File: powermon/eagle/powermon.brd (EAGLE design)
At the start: 50 x 50 mm, 46 parts, among them J1 USB, J3 TERMINAL-2, J6 USB, U1 LTC2943, U2 LT1764AEQ, U3 FT232RLQFN32, U4 ATMEGA328MLF

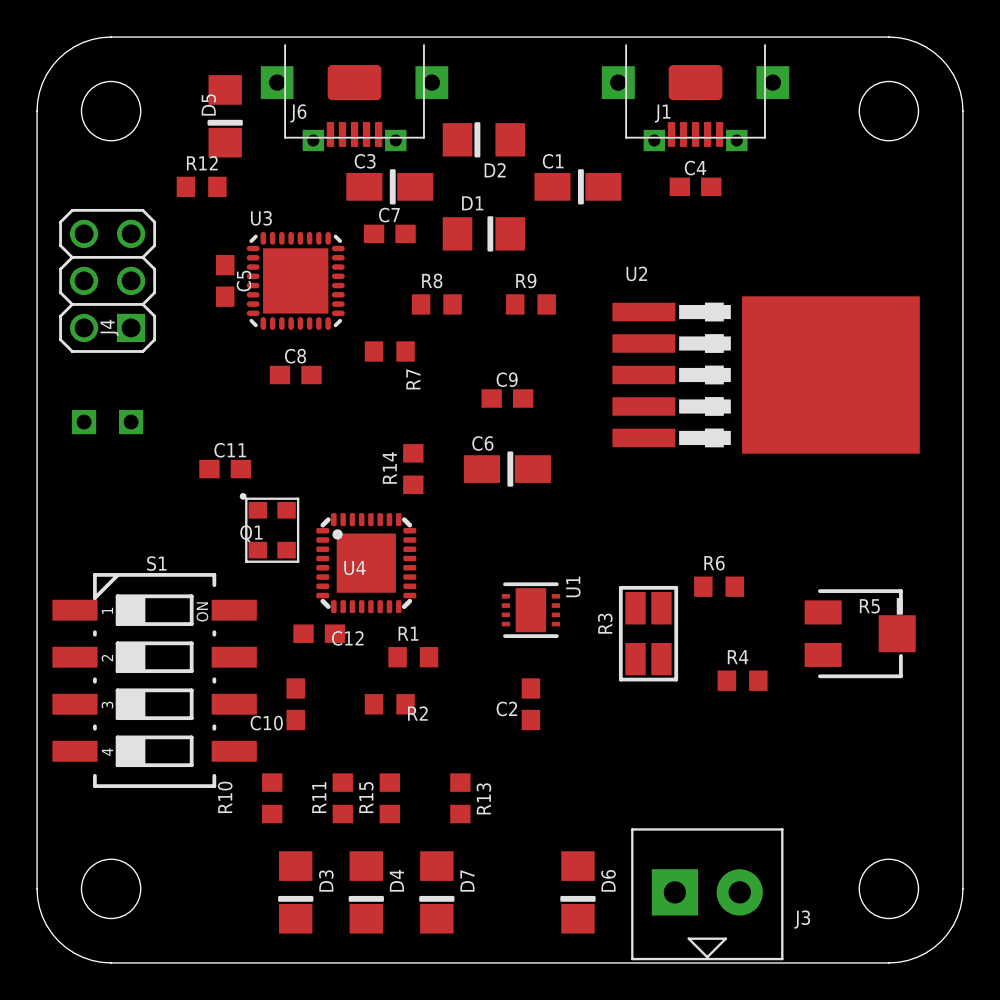
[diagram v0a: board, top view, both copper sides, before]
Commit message: Done initial routing of manual nets. Incomplete.
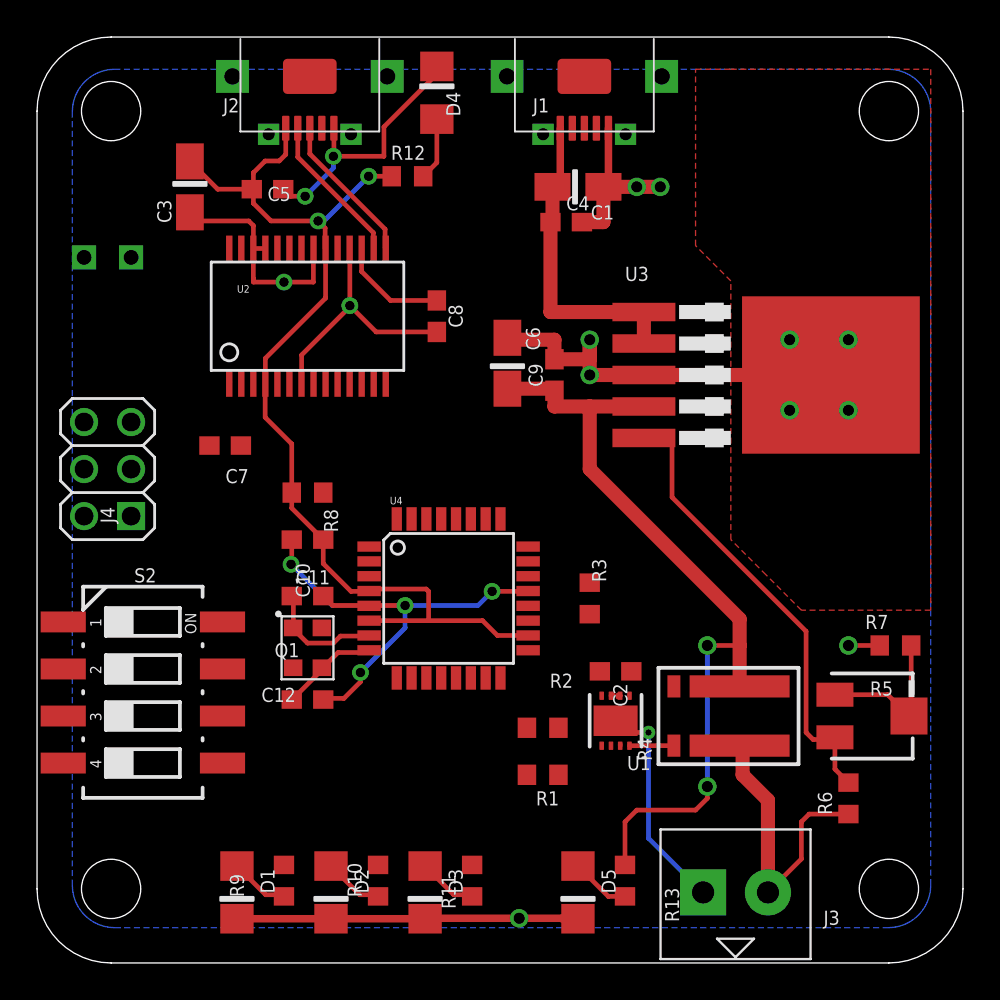
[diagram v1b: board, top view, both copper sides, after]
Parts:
- removed D6: BLUE, powermon:1206-LED
- removed D7: GREEN, powermon:1206-LED
- removed J6: USB, powermon:ZX62RD-AB-5P8
- removed R14: 10K, powermon:R0603
- removed R15: 3.3K, powermon:R0603
- removed S3: PUSH_BUTTON, powermon:DUMMY-2
- added J2: USB, powermon:ZX62RD-AB-5P8
- added S2: 219-04, powermon:CTS-219-04
- D3: value RED -> GREEN
- D4: value GREEN -> BLUE
- R1: value 4.7K -> 10K
- R3: value 0.025R 1% -> 4.7K; device powermon:SHUNT -> powermon:R0603
- R4: value 8K2 1% -> 0.025R 1%; device powermon:R0603 -> powermon:SHUNT
- R6: value 3.3K 1% -> 8K2 1%
- R7: value 10K -> 3.3K 1%
- R8: value 3.3K -> 10K
- S1: value 219-04 -> PUSH_BUTTON; device powermon:CTS-219-04 -> powermon:DUMMY-2
- U2: value LT1764AEQ -> FT232RL; device powermon:TO263-5 -> powermon:SSOP28DB
- U3: value FT232RLQFN32 -> LT1764AEQ; device powermon:QFN32 -> powermon:TO263-5
- U4: value ATMEGA328MLF -> ATMEGA328TQFP32; device powermon:MLF32 -> powermon:TQFP32-08
- moved D5 46.0 mm to (29.2, 3.81)
- moved D4 43.3 mm to (21.6, 47.0), turned to 90 degrees
- moved D2 41.5 mm to (15.9, 3.81), turned to 270 degrees
- moved D1 38.0 mm to (10.8, 3.81), turned to 270 degrees
- moved R9 33.9 mm to (13.3, 4.45), turned to 90 degrees
- moved R7 31.6 mm to (46.4, 17.1)
- moved U3 25.9 mm to (39.4, 31.8), turned to 270 degrees
- moved U2 25.0 mm to (14.6, 34.9), turned to 0 degrees
- moved S1 24.2 mm to (5.08, 39.4), turned to 0 degrees
- moved C7 14.5 mm to (10.2, 27.9), turned to 180 degrees
- moved R6 13.4 mm to (43.8, 8.89), turned to 90 degrees
- moved R8 12.3 mm to (14.6, 25.4), turned to 180 degrees
- moved R12 11.1 mm to (20.0, 42.5)
- moved C3 10.8 mm to (8.26, 41.9), turned to 90 degrees
- moved J4 10.2 mm to (3.81, 26.7)
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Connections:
- removed net GND@3: U1.2, U1.3, U1.7, U1.EXP
- removed net N$12: C3.+, C5.1, J6.1, U3.1, U3.19
- removed net N$21: J1.1
- removed net N$6: D1.A, R8.1
- removed net N$8: D2.A, R9.1
- removed net RX_LED: D2.C, U3.22
- removed net TX_LED: D1.C, U3.21
- net +5V: now also C3.+, C5.1, J2.1, R3.2, U2.20, U2.4; no longer R14.2, R7.2, R9.2
- net ACTION: now also S1.P$1; no longer S3.P$1
- net ACTIVITY_LED: now also R10.2; no longer R11.2
- net CONFIG1: now also S2.8; no longer S1.8
- net CONFIG2: now also S2.7; no longer S1.7
- net CONFIG3: now also S2.6; no longer S1.6
- net CONFIG4: now also S2.5; no longer S1.5
- net DEBUG_LED: now also R11.2; no longer R15.2
- net ERROR_LED: now also R9.2; no longer R10.2
- net GND: now also D1.C, D2.C, J2.5, R7.2, S1.P$2, S2.1, S2.2, S2.3, S2.4, U1.2, U1.3, U1.7, U1.EXP, U2.18, U2.21, U2.25, U2.26, U2.7, U3.3, U3.6; no longer D6.C, D7.C, J6.5, R6.2, S1.1, S1.2, S1.3, S1.4, S3.P$2, U2.3, U2.6, U3.17, U3.20, U3.24, U3.26, U3.4, U3.EXP, U4.EXP
- net I2C-CLK: now also R3.1; no longer R2.1
- net I2C-DATA: now also R2.1; no longer R1.1
- net N$1: now also R1.1; no longer R14.1
- net N$10: now also J2.3, U2.15; no longer J6.3, U3.14
- net N$11: now also U2.2; no longer U3.31
- net N$14: now also D5.A; no longer D6.A
- net N$15: now also J2.2, U2.16; no longer J6.2, U3.15
- net N$16: now also U2.17; no longer U3.16
- net N$17: now also D4.A; no longer D5.A
- net N$18: now also R7.1; no longer R6.1
- net N$19: now also R6.2, U3.5; no longer R4.2, U2.5
- net N$20: now also D3.A, R11.1; no longer D7.A, R15.1
- net N$22: now also R4.I1, R6.1; no longer R3.I1, R4.1
- net N$3: now also D2.A, R10.1; no longer D4.A, R11.1
- net N$4: now also D1.A, R9.1; no longer D3.A, R10.1
- net N$9: now also J1.1, U3.1, U3.2; no longer U2.1, U2.2
- net RESET: now also R8.1; no longer R7.1
- net SENSE+: now also R4.V2; no longer R3.V2
- net SENSE-: now also R4.V1; no longer R3.V1
- net SER_RX: now also U2.1; no longer U3.30
- net SER_TX: now also U2.5; no longer U3.2
- net V+: now also R4.I2, U3.4; no longer R3.I2, U2.4
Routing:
- net GND: track 1.41 -> 135.1 mm, vias 0 -> 19
- net +5V: track 0.00 -> 56.4 mm, vias 0 -> 2
- net V+: track 0.00 -> 45.8 mm, vias 0 -> 2
- net N$19: track 0.00 -> 25.5 mm
- net N$9: track 0.00 -> 16.1 mm
- net N$22: track 0.00 -> 15.8 mm
- net N$18: track 0.00 -> 8.34 mm
- net N$10: track 0.00 -> 8.19 mm
- net N$15: track 0.00 -> 7.70 mm
- net N$2: track 0.00 -> 6.39 mm
- net N$16: track 0.00 -> 5.96 mm
- net N$7: track 0.00 -> 4.82 mm
- net N$20: track 0.00 -> 4.01 mm
- net N$4: track 0.00 -> 4.01 mm
- net N$3: track 0.00 -> 4.01 mm
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- added copper zone on layer 1, net GND
- added copper zone on layer 16, net GND

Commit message: Added footprints, tweaked the placement. Work in progress.
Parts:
- S1: value PUSH_BUTTON -> PUSH_BUTTONEVQPSL; device powermon:DUMMY-2 -> powermon:EVQPSL
- moved S1 3.70 mm to (3.17, 36.2), turned to 180 degrees
- moved J4 2.74 mm to (6.54, 26.5)
- moved C7 1.09 mm to (11.0, 27.3), turned to 270 degrees
- moved S2 0.72 mm to (6.22, 15.1)
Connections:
- net ACTION: now also S1.2.1; no longer S1.P$1
- net GND: now also S1.1.1; no longer S1.P$2
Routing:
- removed copper zone on layer 1, net GND

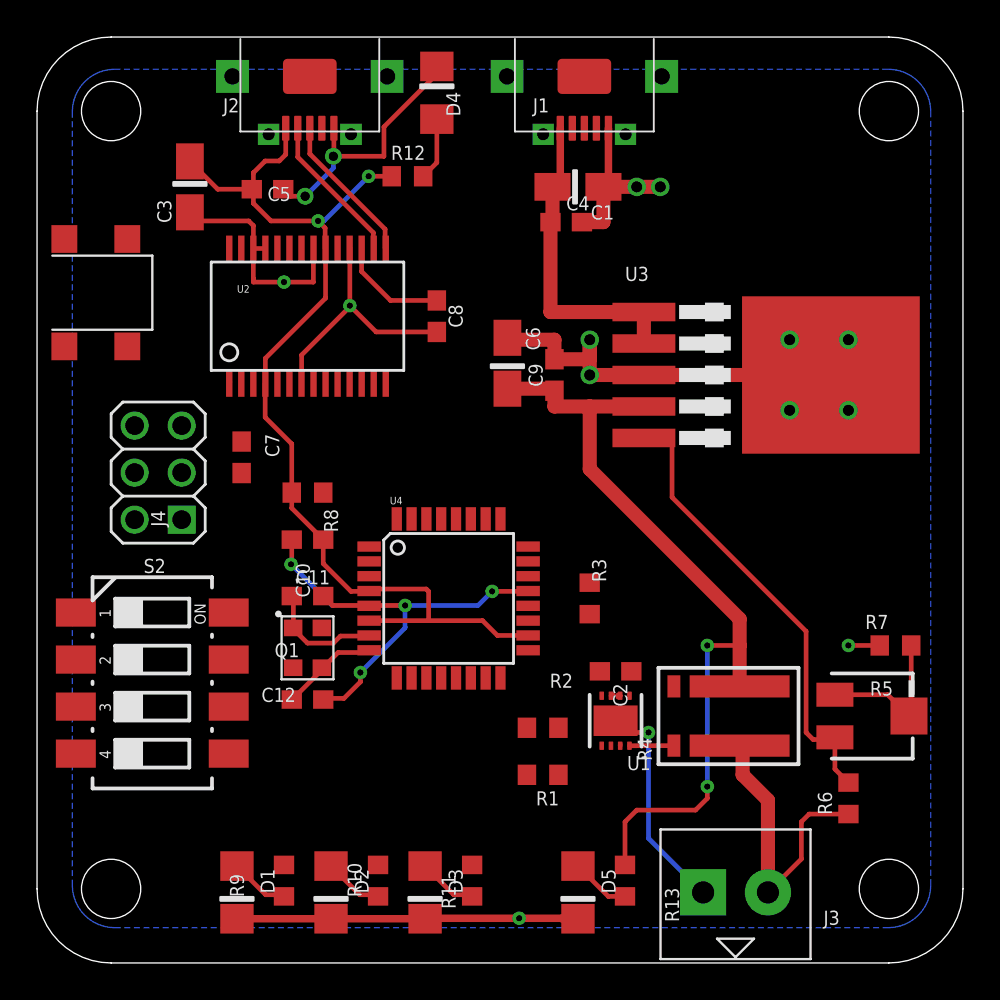
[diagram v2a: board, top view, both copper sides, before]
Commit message: Tweaked the board layout. No DRC. Almost ready for final auto routing.
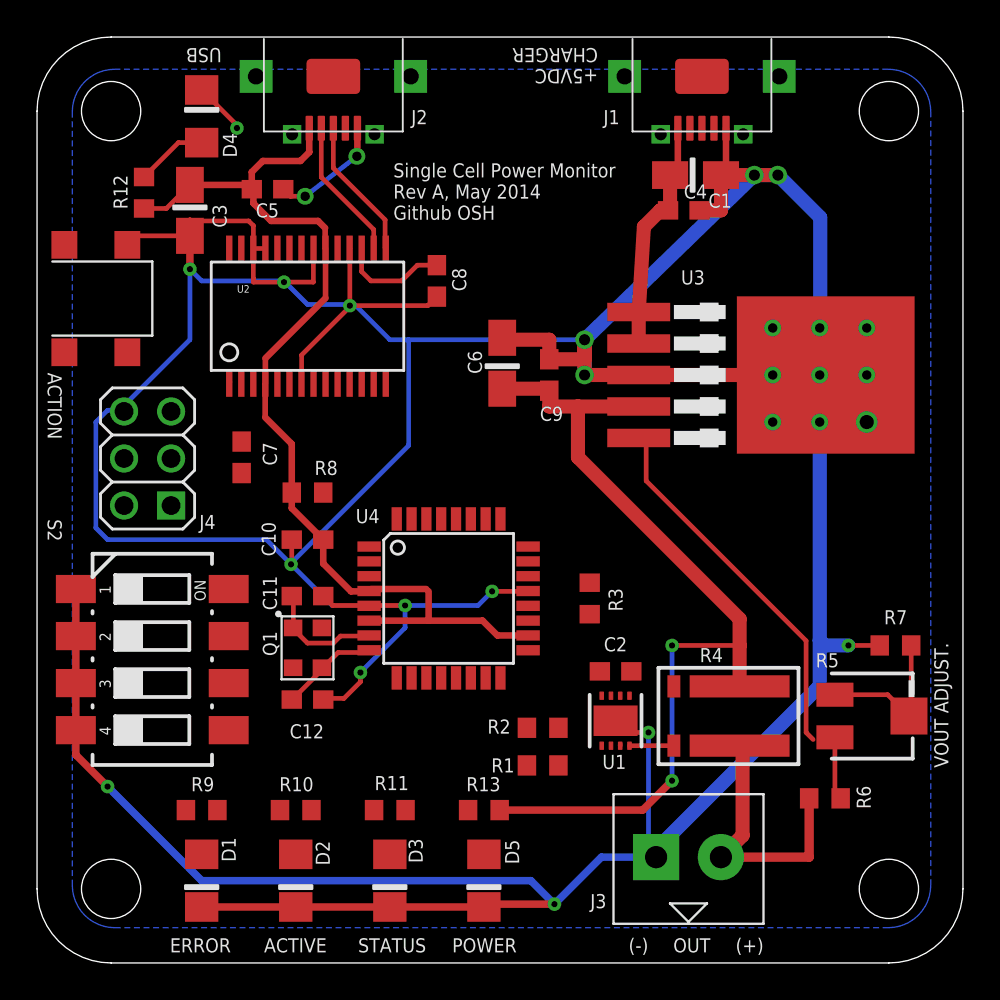
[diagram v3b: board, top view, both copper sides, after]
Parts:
- J1, J2: device powermon:ZX62RD-AB-5P8 -> powermon:USB-MICRO-ZX62RD-AB-5P8
- S1: device powermon:EVQPSL -> powermon:EVQPSL-PUSH-BUTTON
- moved R12 14.3 mm to (5.78, 41.6), turned to 90 degrees
- moved D4 12.8 mm to (8.89, 45.7)
- moved R13 8.52 mm to (24.1, 8.26), turned to 180 degrees
- moved C1 6.38 mm to (35.6, 42.5)
- moved C4 6.38 mm to (34.9, 40.6)
- moved J1 6.35 mm to (35.9, 50.5)
- moved R11 5.85 mm to (19.1, 8.26), turned to 0 degrees
- moved R9 5.85 mm to (8.89, 8.26), turned to 0 degrees
- moved R10 5.85 mm to (14.0, 8.26), turned to 0 degrees
- moved D5 5.12 mm to (24.1, 4.45)
- moved J3 3.17 mm to (35.2, 5.71)
- moved D1 2.01 mm to (8.89, 4.45)
- moved D2 2.01 mm to (14.0, 4.45)
- moved D3 2.01 mm to (19.1, 4.45)
- moved C8 1.91 mm to (21.6, 36.8)
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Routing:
- net GND: track 135.1 -> 326.5 mm, vias 19 -> 27
- net N$9: track 16.1 -> 12.0 mm
- net N$20: track 4.01 -> 0.00 mm
- net N$4: track 4.01 -> 0.00 mm
- net N$3: track 4.01 -> 0.00 mm
- net V+: track 45.8 -> 49.7 mm
- net N$14: track 3.22 -> 0.00 mm
- net N$22: track 15.8 -> 14.5 mm
- net +5V: track 56.4 -> 55.1 mm, vias 2 -> 0
- net N$10: track 8.19 -> 7.67 mm
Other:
- board text added: "(+)"
- board text added: "(-)"
- board text added: "+5VDC CHARGER"
- board text added: "ACTION"
- board text added: "ACTIVE"
- board text added: "ERROR"
- board text added: "OUT"
- board text added: "POWER"
- board text added: "STATUS"
- board text added: "Single Cell Power Monitor Rev A, May 2014 Github OSH"
- board text added: "USB"
- board text added: "VOUT ADJUST."

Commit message: Cleaned up the layout. Should be ready for final auto routing.
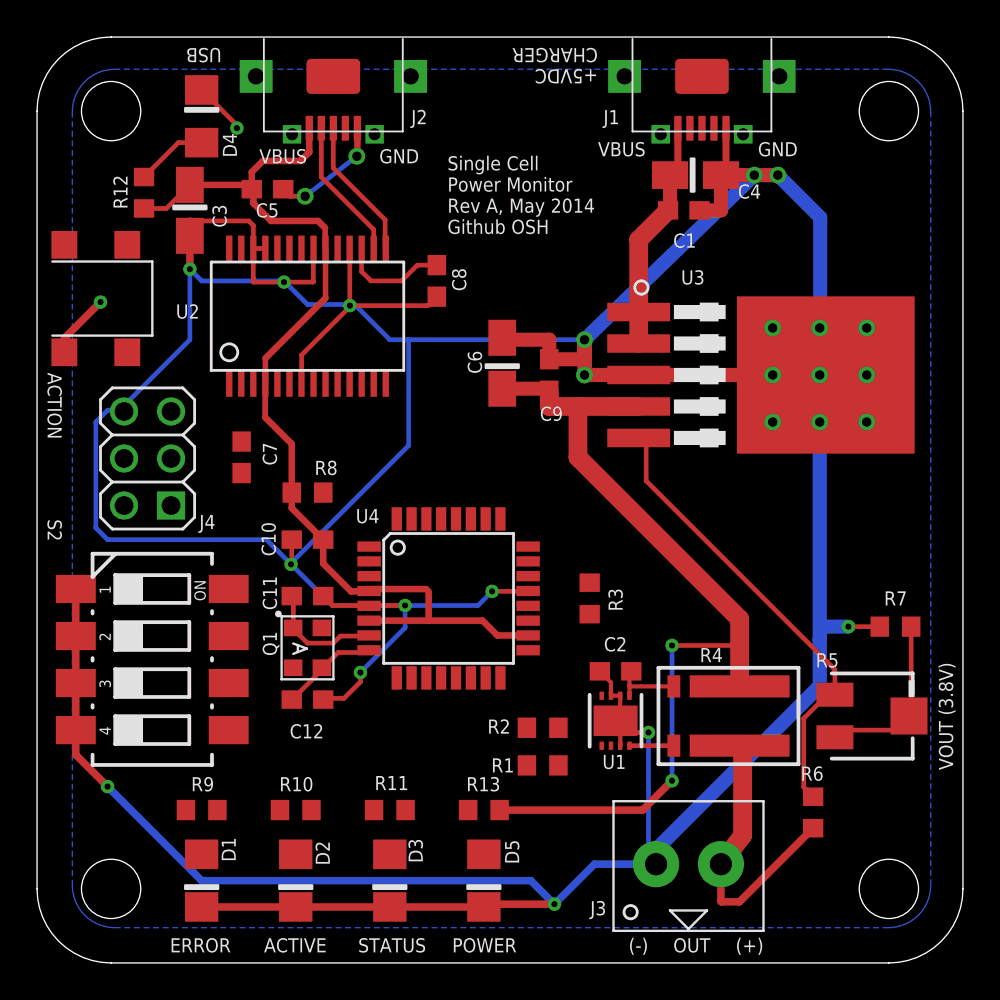
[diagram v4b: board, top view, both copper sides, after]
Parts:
- Q1: device powermon:CTS406 -> powermon:CRYSTAL-CTS406
- R5: device powermon:SM-42/43A -> powermon:TRIM-POT_SM-42/43A
- moved R7 1.02 mm to (46.4, 18.2)
- moved R6 0.99 mm to (41.9, 8.13), turned to 90 degrees
- moved J3 0.38 mm to (35.2, 5.33)
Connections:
- net ACTION: now also S1.1; no longer S1.2.1
- net GND: now also S1.2; no longer S1.1.1
- net N$18: now also R5.1; no longer R5.3
- net N$19: now also R5.3; no longer R5.1
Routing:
- net GND: track 326.5 -> 331.9 mm, vias 27 -> 28
- net SENSE+: track 0.00 -> 3.78 mm
- net N$18: track 8.34 -> 9.59 mm
- net N$22: track 14.5 -> 15.5 mm
- net N$19: track 25.7 -> 26.7 mm
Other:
- board text added: "GND"
- board text added: "VBUS"
- board text added: "VOUT (3.8V)"
- board text removed: "VOUT ADJUST."
